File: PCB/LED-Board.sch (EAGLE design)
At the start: 33 parts, among them U1 ATSAMD11C14A-SSUT, U3 LDL1117S12R

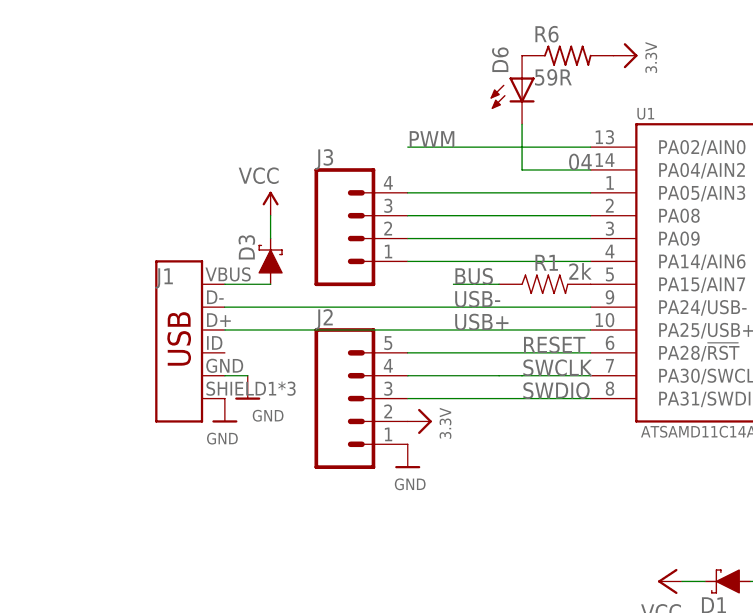
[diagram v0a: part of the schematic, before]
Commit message: added button to pcbs and did some fixing
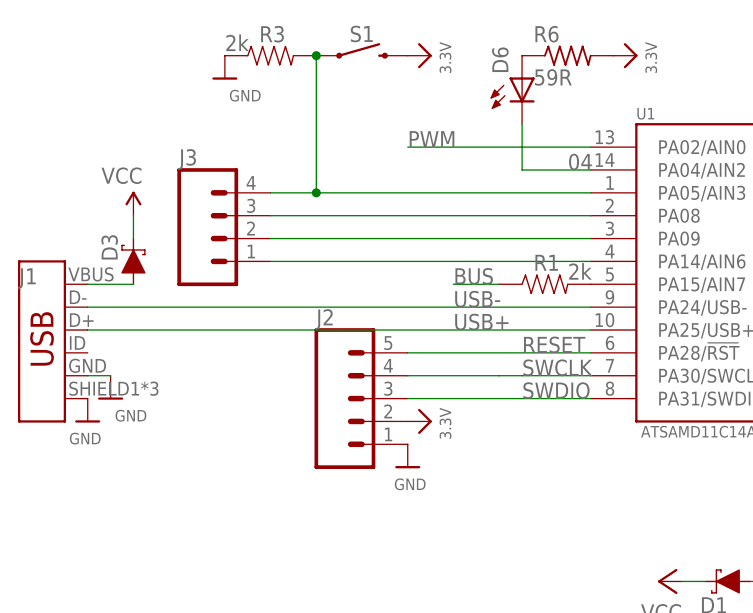
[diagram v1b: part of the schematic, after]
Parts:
- added R3: 2k, SparkFun-Resistors:RESISTOR1206
- added S1: MOMENTARY-SWITCH-SPST-SMD-6.0X3.5MM, SparkFun-Switches:MOMENTARY-SWITCH-SPST-SMD-6.0X3.5MM
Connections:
- removed net N$10: J3.4, U1.PA05/AIN3
- new net N$13: J3.4, R3.2, S1.1, U1.PA05/AIN3
- net 3.3V: now also S1.2
- net GND: now also R3.1
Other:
- moved on the sheet: D3, J1, J3
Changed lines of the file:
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@@
 <?xml version="1.0" encoding="utf-8"?>
 <!DOCTYPE eagle SYSTEM "eagle.dtd">
-<eagle version="9.3.0">
+<eagle version="9.2.2">
 <drawing>
 <settings>
@@
 <part name="FD4" library="SparkFun-Aesthetics" deviceset="FIDUCIAL" device="1X2"/>
 <part name="J2" library="SparkFun-Connectors" deviceset="CONN_05" device=""/>
+<part name="S1" library="SparkFun-Switches" deviceset="MOMENTARY-SWITCH-SPST" device="-SMD-6.0X3.5MM"/>
+<part name="U$11" library="microbuilder" deviceset="3.3V" device=""/>
+<part name="U$14" library="microbuilder" deviceset="GND" device=""/>
+<part name="R3" library="SparkFun-Resistors" deviceset="RESISTOR" device="1206" value="2k"/>
 </parts>
 <sheets>
@@
 <attribute name="VALUE" x="66.548" y="17.145" size="1.778" layer="96"/>
 </instance>
-<instance part="J1" gate="J1" x="-86.36" y="50.8" smashed="yes">
-<attribute name="VALUE" x="-88.9" y="42.926" size="1.778" layer="96" font="vector" align="top-left"/>
-<attribute name="NAME" x="-88.9" y="58.42" size="1.778" layer="95" font="vector"/>
-</instance>
-<instance part="U$5" gate="G$1" x="-78.74" y="45.72" smashed="yes" rot="MR0">
-<attribute name="VALUE" x="-74.676" y="43.18" size="1.27" layer="96" rot="MR0"/>
-</instance>
-<instance part="U$6" gate="G$1" x="-81.28" y="43.18" smashed="yes" rot="MR0">
-<attribute name="VALUE" x="-79.756" y="40.64" size="1.27" layer="96" rot="MR0"/>
-</instance>
-<instance part="SUPPLY2" gate="G$1" x="-76.2" y="66.04" smashed="yes">
-<attribute name="VALUE" x="-79.756" y="69.596" size="1.778" layer="96"/>
-</instance>
-<instance part="D3" gate="G$1" x="-76.2" y="60.96" smashed="yes" rot="R90">
-<attribute name="NAME" x="-77.9526" y="60.96" size="1.778" layer="95" rot="R90"/>
-</instance>
-<instance part="J3" gate="G$1" x="-66.04" y="63.5" smashed="yes">
-<attribute name="VALUE" x="-71.12" y="56.134" size="1.778" layer="96" font="vector"/>
-<attribute name="NAME" x="-71.12" y="71.628" size="1.778" layer="95" font="vector"/>
+<instance part="J1" gate="J1" x="-101.6" y="50.8" smashed="yes">
+<attribute name="VALUE" x="-104.14" y="42.926" size="1.778" layer="96" font="vector" align="top-left"/>
+<attribute name="NAME" x="-104.14" y="58.42" size="1.778" layer="95" font="vector"/>
+</instance>
+<instance part="U$5" gate="G$1" x="-93.98" y="45.72" smashed="yes" rot="MR0">
+<attribute name="VALUE" x="-89.916" y="43.18" size="1.27" layer="96" rot="MR0"/>
+</instance>
+<instance part="U$6" gate="G$1" x="-96.52" y="43.18" smashed="yes" rot="MR0">
+<attribute name="VALUE" x="-94.996" y="40.64" size="1.27" layer="96" rot="MR0"/>
+</instance>
+<instance part="SUPPLY2" gate="G$1" x="-91.44" y="66.04" smashed="yes">
+<attribute name="VALUE" x="-94.996" y="69.596" size="1.778" layer="96"/>
+</instance>
+<instance part="D3" gate="G$1" x="-91.44" y="60.96" smashed="yes" rot="R90">
+<attribute name="NAME" x="-93.1926" y="60.96" size="1.778" layer="95" rot="R90"/>
+</instance>
+<instance part="J3" gate="G$1" x="-81.28" y="63.5" smashed="yes">
+<attribute name="VALUE" x="-86.36" y="56.134" size="1.778" layer="96" font="vector"/>
+<attribute name="NAME" x="-86.36" y="71.628" size="1.778" layer="95" font="vector"/>
 </instance>
 <instance part="C2" gate="G$1" x="7.62" y="30.48" smashed="yes">
@@
 <attribute name="VALUE" x="-71.12" y="35.814" size="1.778" layer="96" font="vector"/>
 <attribute name="NAME" x="-71.12" y="53.848" size="1.778" layer="95" font="vector"/>
+</instance>
+<instance part="S1" gate="G$1" x="-66.04" y="83.82" smashed="yes">
+<attribute name="NAME" x="-66.04" y="85.344" size="1.778" layer="95" font="vector" align="bottom-center"/>
+</instance>
+<instance part="U$11" gate="G$1" x="-58.42" y="83.82" smashed="yes" rot="R270">
+<attribute name="VALUE" x="-57.404" y="85.344" size="1.27" layer="96" rot="R270"/>
+</instance>
+<instance part="U$14" gate="G$1" x="-81.28" y="81.28" smashed="yes" rot="MR0">
+<attribute name="VALUE" x="-77.216" y="78.74" size="1.27" layer="96" rot="MR0"/>
+</instance>
+<instance part="R3" gate="G$1" x="-76.2" y="83.82" smashed="yes">
+<attribute name="NAME" x="-77.47" y="85.3186" size="1.778" layer="95"/>
+<attribute name="VALUE" x="-81.28" y="84.328" size="1.778" layer="96"/>
 </instance>
 </instances>
@@
 <pinref part="SUPPLY2" gate="G$1" pin="VCC"/>
 <pinref part="D3" gate="G$1" pin="C"/>
-<wire x1="-76.2" y1="66.04" x2="-76.2" y2="63.5" width="0.1524" layer="91"/>
+<wire x1="-91.44" y1="66.04" x2="-91.44" y2="63.5" width="0.1524" layer="91"/>
 </segment>
 <segment>
@@
 <pinref part="J1" gate="J1" pin="GND"/>
 <pinref part="U$5" gate="G$1" pin="GND"/>
-<wire x1="-78.74" y1="48.26" x2="-81.28" y2="48.26" width="0.1524" layer="91"/>
+<wire x1="-93.98" y1="48.26" x2="-96.52" y2="48.26" width="0.1524" layer="91"/>
 </segment>
 <segment>
@@
 <pinref part="J2" gate="G$1" pin="1"/>
 <pinref part="U$12" gate="G$1" pin="GND"/>
+</segment>
+<segment>
+<pinref part="R3" gate="G$1" pin="1"/>
+<pinref part="U$14" gate="G$1" pin="GND"/>
 </segment>
 </net>
@@
 <net name="USB+" class="0">
 <segment>
-<wire x1="-81.28" y1="53.34" x2="-40.64" y2="53.34" width="0.1524" layer="91"/>
+<wire x1="-96.52" y1="53.34" x2="-40.64" y2="53.34" width="0.1524" layer="91"/>
 <pinref part="U1" gate="G$1" pin="PA25/USB+"/>
 <label x="-55.88" y="53.34" size="1.778" layer="95"/>
@@
 <net name="USB-" class="0">
 <segment>
-<wire x1="-81.28" y1="55.88" x2="-40.64" y2="55.88" width="0.1524" layer="91"/>
+<wire x1="-96.52" y1="55.88" x2="-40.64" y2="55.88" width="0.1524" layer="91"/>
 <pinref part="U1" gate="G$1" pin="PA24/USB-"/>
 <label x="-55.88" y="55.88" size="1.778" layer="95"/>
@@
 <pinref part="J2" gate="G$1" pin="2"/>
 </segment>
+<segment>
+<pinref part="S1" gate="G$1" pin="2"/>
+<pinref part="U$11" gate="G$1" pin="3.3V"/>
+</segment>
 </net>
 <net name="SWDIO" class="0">
@@
 <segment>
 <pinref part="J1" gate="J1" pin="VBUS"/>
-<wire x1="-76.2" y1="58.42" x2="-81.28" y2="58.42" width="0.1524" layer="91"/>
+<wire x1="-91.44" y1="58.42" x2="-96.52" y2="58.42" width="0.1524" layer="91"/>
 <pinref part="D3" gate="G$1" pin="A"/>
 </segment>
@@
 <pinref part="U1" gate="G$1" pin="PA14/AIN6"/>
 <pinref part="J3" gate="G$1" pin="1"/>
-<wire x1="-60.96" y1="60.96" x2="-40.64" y2="60.96" width="0.1524" layer="91"/>
+<wire x1="-76.2" y1="60.96" x2="-40.64" y2="60.96" width="0.1524" layer="91"/>
 </segment>
 </net>
@@
 <pinref part="U1" gate="G$1" pin="PA09"/>
 <pinref part="J3" gate="G$1" pin="2"/>
-<wire x1="-60.96" y1="63.5" x2="-40.64" y2="63.5" width="0.1524" layer="91"/>
+<wire x1="-76.2" y1="63.5" x2="-40.64" y2="63.5" width="0.1524" layer="91"/>
 </segment>
 </net>
@@
 <pinref part="U1" gate="G$1" pin="PA08"/>
 <pinref part="J3" gate="G$1" pin="3"/>
-<wire x1="-60.96" y1="66.04" x2="-40.64" y2="66.04" width="0.1524" layer="91"/>
-</segment>
-</net>
-<net name="N$10" class="0">
-<segment>
-<pinref part="U1" gate="G$1" pin="PA05/AIN3"/>
-<pinref part="J3" gate="G$1" pin="4"/>
-<wire x1="-60.96" y1="68.58" x2="-40.64" y2="68.58" width="0.1524" layer="91"/>
+<wire x1="-76.2" y1="66.04" x2="-40.64" y2="66.04" width="0.1524" layer="91"/>
 </segment>
 </net>
@@
 </segment>
 </net>
+<net name="N$13" class="0">
+<segment>
+<pinref part="S1" gate="G$1" pin="1"/>
+<pinref part="R3" gate="G$1" pin="2"/>
+<pinref part="U1" gate="G$1" pin="PA05/AIN3"/>
+<pinref part="J3" gate="G$1" pin="4"/>
+<wire x1="-76.2" y1="68.58" x2="-71.12" y2="68.58" width="0.1524" layer="91"/>
+<wire x1="-71.12" y1="68.58" x2="-40.64" y2="68.58" width="0.1524" layer="91"/>
+<wire x1="-71.12" y1="83.82" x2="-71.12" y2="68.58" width="0.1524" layer="91"/>
+<junction x="-71.12" y="83.82"/>
+<junction x="-71.12" y="68.58"/>
+</segment>
+</net>

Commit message: removed buttons.. not needed
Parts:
- removed R3: 2k, SparkFun-Resistors:RESISTOR1206
- removed S1: MOMENTARY-SWITCH-SPST-SMD-6.0X3.5MM, SparkFun-Switches:MOMENTARY-SWITCH-SPST-SMD-6.0X3.5MM
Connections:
- net 3.3V: no longer S1.2
- net GND: no longer R3.1
- net N$13: no longer R3.2, S1.1
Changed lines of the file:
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@@
 <?xml version="1.0" encoding="utf-8"?>
 <!DOCTYPE eagle SYSTEM "eagle.dtd">
-<eagle version="9.2.2">
+<eagle version="9.3.0">
 <drawing>
 <settings>
@@
 <part name="FD4" library="SparkFun-Aesthetics" deviceset="FIDUCIAL" device="1X2"/>
 <part name="J2" library="SparkFun-Connectors" deviceset="CONN_05" device=""/>
-<part name="S1" library="SparkFun-Switches" deviceset="MOMENTARY-SWITCH-SPST" device="-SMD-6.0X3.5MM"/>
-<part name="U$11" library="microbuilder" deviceset="3.3V" device=""/>
-<part name="U$14" library="microbuilder" deviceset="GND" device=""/>
-<part name="R3" library="SparkFun-Resistors" deviceset="RESISTOR" device="1206" value="2k"/>
 </parts>
 <sheets>
@@
 <attribute name="VALUE" x="-71.12" y="35.814" size="1.778" layer="96" font="vector"/>
 <attribute name="NAME" x="-71.12" y="53.848" size="1.778" layer="95" font="vector"/>
-</instance>
-<instance part="S1" gate="G$1" x="-66.04" y="83.82" smashed="yes">
-<attribute name="NAME" x="-66.04" y="85.344" size="1.778" layer="95" font="vector" align="bottom-center"/>
-</instance>
-<instance part="U$11" gate="G$1" x="-58.42" y="83.82" smashed="yes" rot="R270">
-<attribute name="VALUE" x="-57.404" y="85.344" size="1.27" layer="96" rot="R270"/>
-</instance>
-<instance part="U$14" gate="G$1" x="-81.28" y="81.28" smashed="yes" rot="MR0">
-<attribute name="VALUE" x="-77.216" y="78.74" size="1.27" layer="96" rot="MR0"/>
-</instance>
-<instance part="R3" gate="G$1" x="-76.2" y="83.82" smashed="yes">
-<attribute name="NAME" x="-77.47" y="85.3186" size="1.778" layer="95"/>
-<attribute name="VALUE" x="-81.28" y="84.328" size="1.778" layer="96"/>
 </instance>
 </instances>
@@
 <pinref part="U$12" gate="G$1" pin="GND"/>
 </segment>
-<segment>
-<pinref part="R3" gate="G$1" pin="1"/>
-<pinref part="U$14" gate="G$1" pin="GND"/>
-</segment>
 </net>
 <net name="LED-" class="0">
@@
 <pinref part="J2" gate="G$1" pin="2"/>
 </segment>
-<segment>
-<pinref part="S1" gate="G$1" pin="2"/>
-<pinref part="U$11" gate="G$1" pin="3.3V"/>
-</segment>
 </net>
 <net name="SWDIO" class="0">
@@
 <net name="N$13" class="0">
 <segment>
-<pinref part="S1" gate="G$1" pin="1"/>
-<pinref part="R3" gate="G$1" pin="2"/>
 <pinref part="U1" gate="G$1" pin="PA05/AIN3"/>
 <pinref part="J3" gate="G$1" pin="4"/>
-<wire x1="-76.2" y1="68.58" x2="-71.12" y2="68.58" width="0.1524" layer="91"/>
-<wire x1="-71.12" y1="68.58" x2="-40.64" y2="68.58" width="0.1524" layer="91"/>
-<wire x1="-71.12" y1="83.82" x2="-71.12" y2="68.58" width="0.1524" layer="91"/>
-<junction x="-71.12" y="83.82"/>
-<junction x="-71.12" y="68.58"/>
-</segment>
-</net>
+<wire x1="-76.2" y1="68.58" x2="-40.64" y2="68.58" width="0.1524" layer="91"/>
+</segment>
+</net>
